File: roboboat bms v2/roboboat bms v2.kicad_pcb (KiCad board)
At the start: 4 copper layers, 47 x 62.5 mm, 37 parts, among them J1 Conn_01x04_Pin, J3 XT90PW-F, J4 XT90PW-M, J6 B5B-XH-A, J7 JST_XH Thermistor 2 Pin Conne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, Q1 IRFP4468PbF, Q3 BSS84, Q5 IRFP4468PbF, SW1 SW_Push, U1 BQ76920PW

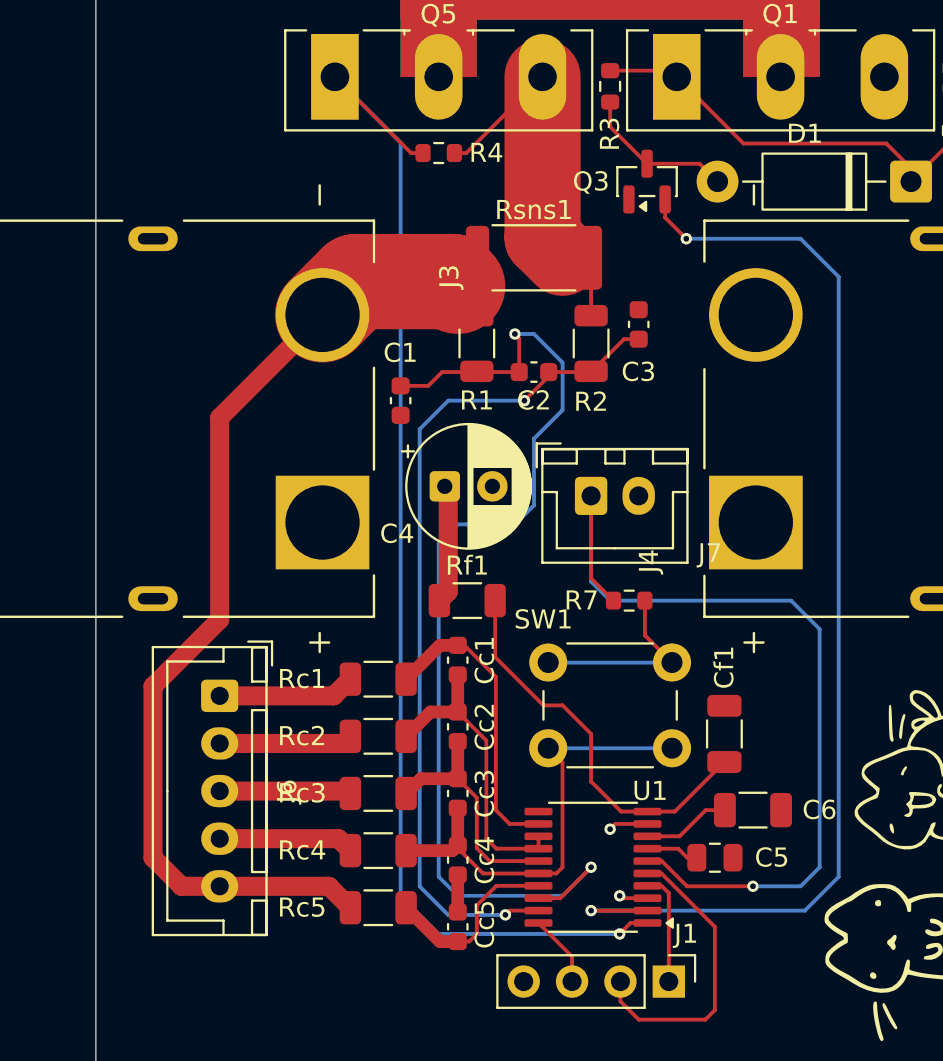
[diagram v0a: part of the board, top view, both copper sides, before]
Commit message: update MOSFET to IRF7430
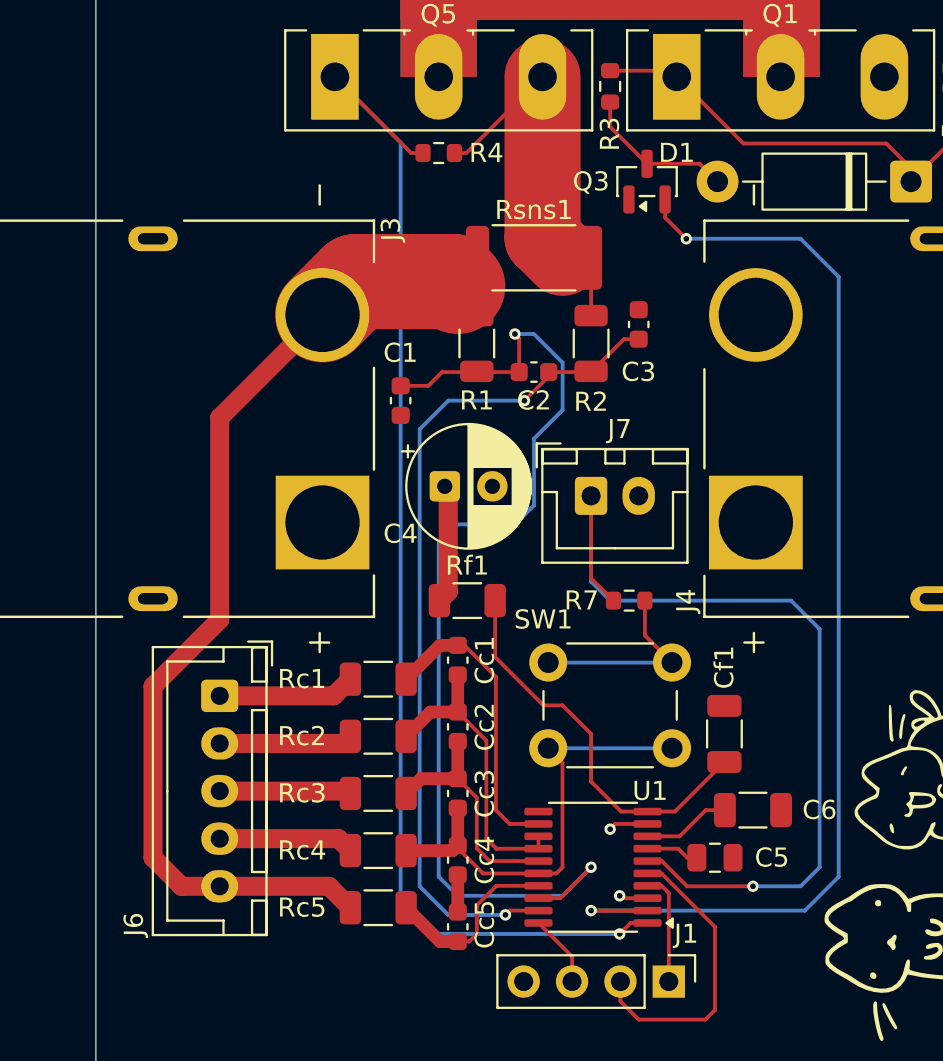
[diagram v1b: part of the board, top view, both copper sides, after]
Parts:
- Q1, Q5: value IRFP4468PbF -> IRFP7430PBF
